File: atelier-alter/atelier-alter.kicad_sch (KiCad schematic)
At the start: 55 parts, among them SW1 SW_DPST, SW2 SW_DPST, SW3 SW_DPST, SW4 RESET, U1 ATmega32U4-A, U2 PRTR5V0U2X, Y1 16Mhz

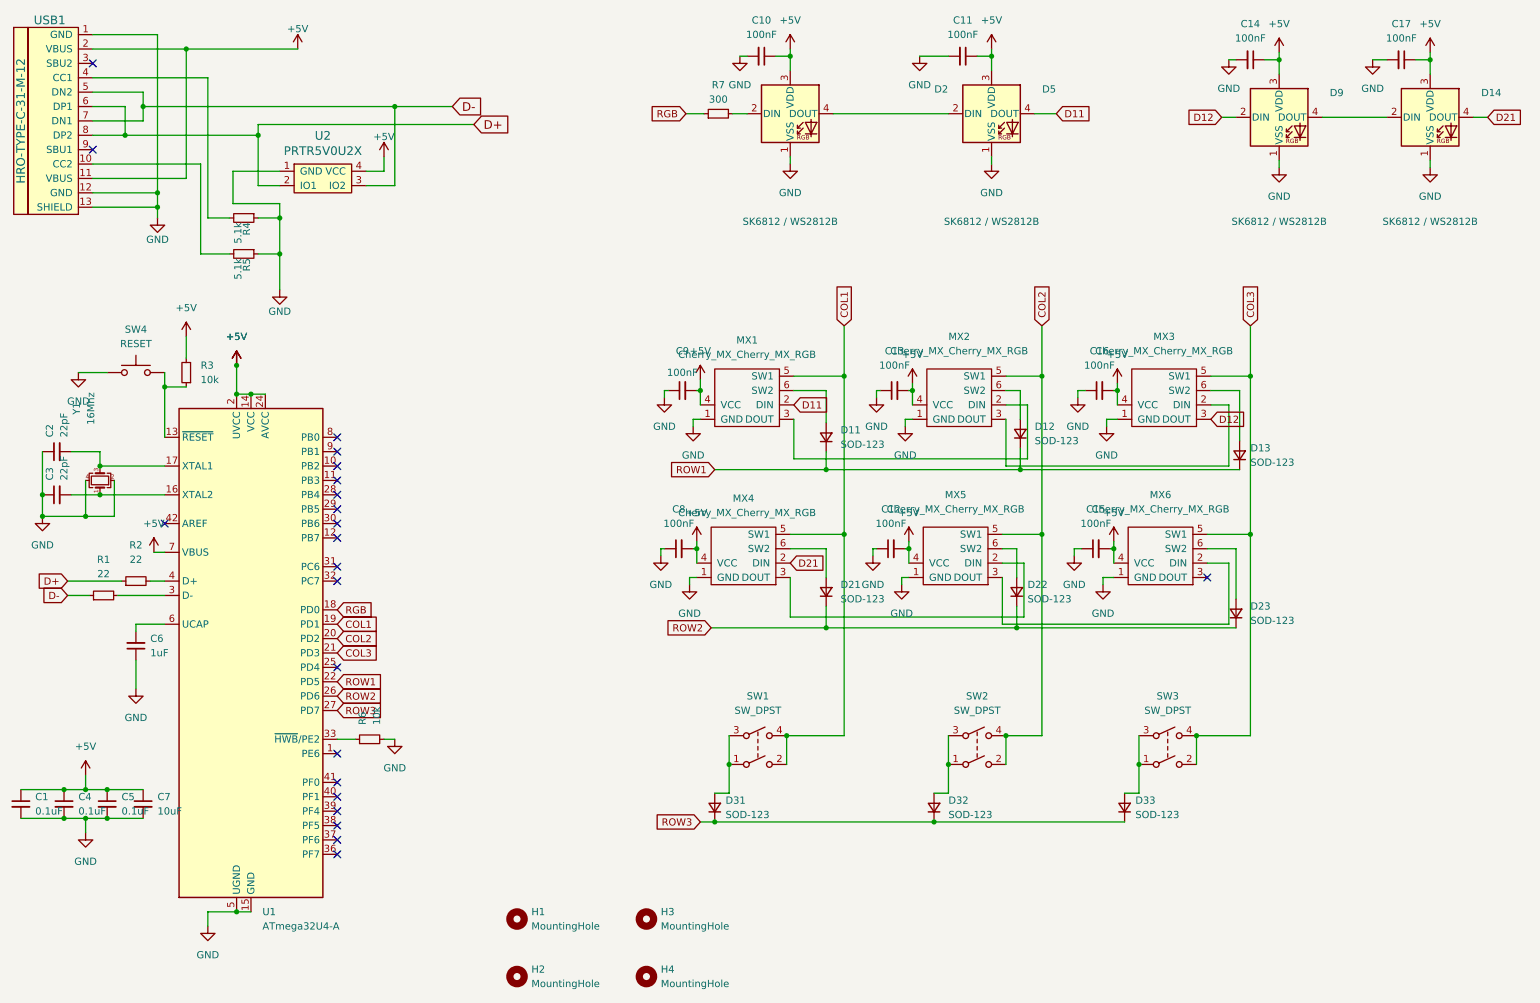
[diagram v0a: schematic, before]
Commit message: decided to nuke all led capacitor
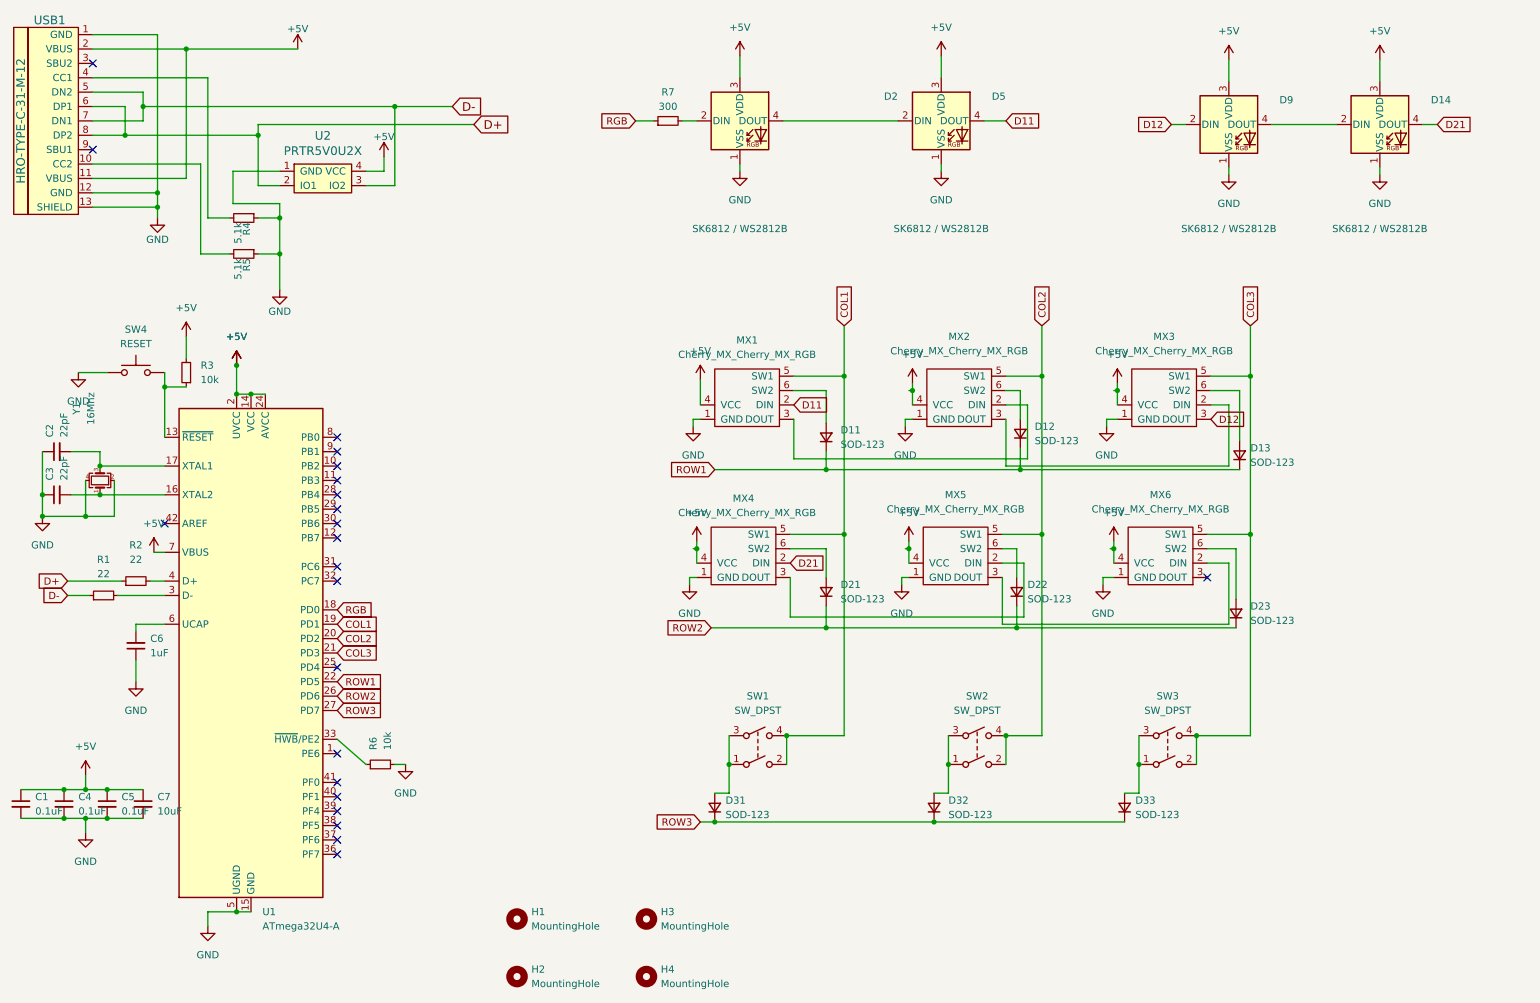
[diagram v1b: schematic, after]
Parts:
- removed C10, C11, C12, C13, C14, C15, C16, C17, C8, C9: 100nF, Capacitor_SMD:C_0805_2012Metric, symbol Device:C_Small
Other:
- moved on the sheet: D14, D2, D5, D9, R6, R7

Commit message: update pcb + qmk firmware
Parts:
- added R8: 300, Resistor_SMD:R_0805_2012Metric, symbol Device:R_Small
- renumbered D2 to D1, D5 to D2, D9 to D3, D14 to D4
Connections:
- net D12: now also MX4.2 (DIN); no longer D3.2 (DIN)
- net at U1.25 (PD4): now also R8.1
- net BackRGB: now reaches D1.2 (DIN)
- net BackRGB: now also R8.2; no longer R7.2
- net D11: no longer names the net of D2.4 (DOUT)
- net D11: now also D3.2 (DIN); no longer MX1.2 (DIN)
- net D21: no longer names the net of D4.4 (DOUT)
- net D21: no longer MX4.2 (DIN)
- net RGB: no longer names the net of R7.1, U1.18 (PD0)
- new net InKeyRGB: MX1.2 (DIN), R7.2
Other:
- moved on the sheet: D1, D3, D4

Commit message: final commit for rev 0.
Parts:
- H1, H2, H3, H4: footprint MountingHole:MountingHole_5.3mm_M5 -> MountingHole:MountingHole_3.2mm_M3_ISO7380
- R1, R2: footprint Resistor_SMD:R_0805_2012Metric -> Resistor_SMD:R_0603_1608Metric_Pad0.98x0.95mm_HandSolder
- SW1, SW2, SW3: footprint Button_Switch_THT:SW_PUSH_6mm_H9.5mm -> Button_Switch_THT:SW_PUSH_6mm_H13mm
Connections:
- net at U1.25 (PD4): no longer R8.1
- net at U1.28 (PB4): now also R8.1
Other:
- moved on the sheet: R8
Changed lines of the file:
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@@
   )
   (no_connect (at 31.75 40.64))
-  (no_connect (at 74.93 104.14))
   (no_connect (at 74.93 106.68))
   (no_connect (at 238.125 35.56))
+  (no_connect (at 74.93 132.08))
   (no_connect (at 74.93 152.4))
   (no_connect (at 44.45 106.68))
@@
   (no_connect (at 74.93 99.06))
   (no_connect (at 31.75 25.4))
+  (no_connect (at 74.93 104.14))
   (no_connect (at 228.6 116.205))
-  (no_connect (at 74.93 101.6))
   (wire (pts (xy 52.07 177.8) (xy 52.07 175.26))
     (stroke (width 0) (type default) (color 0 0 0 0))
@@
     (stroke (width 0) (type default) (color 0 0 0 0))
   )
+  (wire (pts (xy 76.835 101.6) (xy 74.93 101.6))
+    (stroke (width 0) (type default) (color 0 0 0 0))
+  )
   (wire (pts (xy 232.41 124.46) (xy 232.41 113.665))
     (stroke (width 0) (type default) (color 0 0 0 0))
@@
     (stroke (width 0) (type default) (color 0 0 0 0))
   )
-  (wire (pts (xy 86.995 132.08) (xy 83.185 132.08))
+  (wire (pts (xy 85.725 101.6) (xy 81.915 101.6))
     (stroke (width 0) (type default) (color 0 0 0 0))
   )
@@
   )
   (wire (pts (xy 180.34 154.305) (xy 182.88 154.305))
-    (stroke (width 0) (type default) (color 0 0 0 0))
-  )
-  (wire (pts (xy 78.105 132.08) (xy 74.93 132.08))
     (stroke (width 0) (type default) (color 0 0 0 0))
   )
@@
     )
   )
-  (global_label "BackRGB" (shape input) (at 86.995 132.08 0) (fields_autoplaced)
+  (global_label "BackRGB" (shape input) (at 85.725 101.6 0) (fields_autoplaced)
     (effects (font (size 1.27 1.27)) (justify left))
-    (property "Intersheet References" "${INTERSHEET_REFS}" (id 0) (at 97.7538 132.0006 0)
+    (property "Intersheet References" "${INTERSHEET_REFS}" (id 0) (at 96.4838 101.5206 0)
       (effects (font (size 1.27 1.27)) (justify left) hide)
     )
@@
     (property "Reference" "SW3" (id 0) (at 221.615 137.16 0))
     (property "Value" "SW_DPST" (id 1) (at 221.615 139.7 0))
-    (property "Footprint" "Button_Switch_THT:SW_PUSH_6mm_H9.5mm" (id 2) (at 221.615 146.685 0)
+    (property "Footprint" "Button_Switch_THT:SW_PUSH_6mm_H13mm" (id 2) (at 221.615 146.685 0)
       (effects (font (size 1.27 1.27)) hide)
     )
@@
       (effects (font (size 1.27 1.27)) (justify left))
     )
-    (property "Footprint" "MountingHole:MountingHole_5.3mm_M5" (id 2) (at 129.54 186.69 0)
+    (property "Footprint" "MountingHole:MountingHole_3.2mm_M3_ISO7380" (id 2) (at 129.54 186.69 0)
       (effects (font (size 1.27 1.27)) hide)
     )
@@
       (effects (font (size 1.27 1.27)) (justify left))
     )
-    (property "Footprint" "MountingHole:MountingHole_5.3mm_M5" (id 2) (at 106.68 186.69 0)
+    (property "Footprint" "MountingHole:MountingHole_3.2mm_M3_ISO7380" (id 2) (at 106.68 186.69 0)
       (effects (font (size 1.27 1.27)) hide)
     )
@@
     (property "Reference" "R2" (id 0) (at 39.37 110.49 90))
     (property "Value" "22" (id 1) (at 39.37 113.03 90))
-    (property "Footprint" "Resistor_SMD:R_0805_2012Metric" (id 2) (at 39.37 116.84 0)
+    (property "Footprint" "Resistor_SMD:R_0603_1608Metric_Pad0.98x0.95mm_HandSolder" (id 2) (at 39.37 116.84 0)
       (effects (font (size 1.27 1.27)) hide)
     )
@@
     (pin "1")
   )
-  (symbol (lib_id "Device:R_Small") (at 80.645 132.08 90) (unit 1)
+  (symbol (lib_id "Device:R_Small") (at 79.375 101.6 90) (unit 1)
     (in_bom yes) (on_board yes)
-    (property "Reference" "R8" (id 0) (at 80.645 127 90))
-    (property "Value" "300" (id 1) (at 80.645 129.54 90))
-    (property "Footprint" "Resistor_SMD:R_0805_2012Metric" (id 2) (at 80.645 132.08 0)
-      (effects (font (size 1.27 1.27)) hide)
-    )
-    (property "Datasheet" "~" (id 3) (at 80.645 132.08 0)
+    (property "Reference" "R8" (id 0) (at 79.375 96.52 90))
+    (property "Value" "300" (id 1) (at 79.375 99.06 90))
+    (property "Footprint" "Resistor_SMD:R_0805_2012Metric" (id 2) (at 79.375 101.6 0)
+      (effects (font (size 1.27 1.27)) hide)
+    )
+    (property "Datasheet" "~" (id 3) (at 79.375 101.6 0)
       (effects (font (size 1.27 1.27)) hide)
     )
@@
       (effects (font (size 1.27 1.27)) (justify left))
     )
-    (property "Footprint" "MountingHole:MountingHole_5.3mm_M5" (id 2) (at 106.68 176.53 0)
+    (property "Footprint" "MountingHole:MountingHole_3.2mm_M3_ISO7380" (id 2) (at 106.68 176.53 0)
       (effects (font (size 1.27 1.27)) hide)
     )
@@
       (effects (font (size 1.27 1.27)) (justify left))
     )
-    (property "Footprint" "MountingHole:MountingHole_5.3mm_M5" (id 2) (at 129.54 176.53 0)
+    (property "Footprint" "MountingHole:MountingHole_3.2mm_M3_ISO7380" (id 2) (at 129.54 176.53 0)
       (effects (font (size 1.27 1.27)) hide)
     )
@@
     (property "Reference" "SW1" (id 0) (at 149.225 137.16 0))
     (property "Value" "SW_DPST" (id 1) (at 149.225 139.7 0))
-    (property "Footprint" "Button_Switch_THT:SW_PUSH_6mm_H9.5mm" (id 2) (at 149.225 146.685 0)
+    (property "Footprint" "Button_Switch_THT:SW_PUSH_6mm_H13mm" (id 2) (at 149.225 146.685 0)
       (effects (font (size 1.27 1.27)) hide)
     )
@@
     (property "Reference" "R1" (id 0) (at 33.655 113.03 90))
     (property "Value" "22" (id 1) (at 33.655 115.57 90))
-    (property "Footprint" "Resistor_SMD:R_0805_2012Metric" (id 2) (at 33.655 119.38 0)
+    (property "Footprint" "Resistor_SMD:R_0603_1608Metric_Pad0.98x0.95mm_HandSolder" (id 2) (at 33.655 119.38 0)
       (effects (font (size 1.27 1.27)) hide)
     )
@@
     (property "Reference" "SW2" (id 0) (at 187.96 137.16 0))
     (property "Value" "SW_DPST" (id 1) (at 187.96 139.7 0))
-    (property "Footprint" "Button_Switch_THT:SW_PUSH_6mm_H9.5mm" (id 2) (at 187.96 146.685 0)
+    (property "Footprint" "Button_Switch_THT:SW_PUSH_6mm_H13mm" (id 2) (at 187.96 146.685 0)
       (effects (font (size 1.27 1.27)) hide)
     )
@@
     )
     (path "/8556b1bc-59f1-44d9-99ff-e1f2c0ffcf36"
-      (reference "H1") (unit 1) (value "MountingHole") (footprint "MountingHole:MountingHole_5.3mm_M5")
+      (reference "H1") (unit 1) (value "MountingHole") (footprint "MountingHole:MountingHole_3.2mm_M3_ISO7380")
     )
     (path "/5a99e80a-11b8-48d3-b554-660c0bcf5c38"
-      (reference "H2") (unit 1) (value "MountingHole") (footprint "MountingHole:MountingHole_5.3mm_M5")
+      (reference "H2") (unit 1) (value "MountingHole") (footprint "MountingHole:MountingHole_3.2mm_M3_ISO7380")
     )
     (path "/9a99f614-4356-46fa-a338-e647cb700704"
-      (reference "H3") (unit 1) (value "MountingHole") (footprint "MountingHole:MountingHole_5.3mm_M5")
+      (reference "H3") (unit 1) (value "MountingHole") (footprint "MountingHole:MountingHole_3.2mm_M3_ISO7380")
     )
     (path "/3b67de7c-1c99-408a-a31c-508b13725aa4"
-      (reference "H4") (unit 1) (value "MountingHole") (footprint "MountingHole:MountingHole_5.3mm_M5")
+      (reference "H4") (unit 1) (value "MountingHole") (footprint "MountingHole:MountingHole_3.2mm_M3_ISO7380")
     )
     (path "/92fbf038-747f-4dcc-ac4a-6dcc9e81a6d6"
@@
     )
     (path "/cab66ac1-fa01-4b4d-b047-bbf2c7667c4d"
-      (reference "R1") (unit 1) (value "22") (footprint "Resistor_SMD:R_0805_2012Metric")
+      (reference "R1") (unit 1) (value "22") (footprint "Resistor_SMD:R_0603_1608Metric_Pad0.98x0.95mm_HandSolder")
     )
     (path "/7a828e50-c71e-4f23-a75f-5b21626200ef"
-      (reference "R2") (unit 1) (value "22") (footprint "Resistor_SMD:R_0805_2012Metric")
+      (reference "R2") (unit 1) (value "22") (footprint "Resistor_SMD:R_0603_1608Metric_Pad0.98x0.95mm_HandSolder")
     )
     (path "/ab650c07-16c5-47e1-91d8-64187369346c"
@@
     )
     (path "/a25abf13-8d9c-45bf-8510-20336f41d055"
-      (reference "SW1") (unit 1) (value "SW_DPST") (footprint "Button_Switch_THT:SW_PUSH_6mm_H9.5mm")
+      (reference "SW1") (unit 1) (value "SW_DPST") (footprint "Button_Switch_THT:SW_PUSH_6mm_H13mm")
     )
     (path "/ecfd7051-baf1-4abd-8967-31e1a5902ed8"
-      (reference "SW2") (unit 1) (value "SW_DPST") (footprint "Button_Switch_THT:SW_PUSH_6mm_H9.5mm")
+      (reference "SW2") (unit 1) (value "SW_DPST") (footprint "Button_Switch_THT:SW_PUSH_6mm_H13mm")
     )
     (path "/09679efe-a303-405b-973d-0bd9043f5a9f"
-      (reference "SW3") (unit 1) (value "SW_DPST") (footprint "Button_Switch_THT:SW_PUSH_6mm_H9.5mm")
+      (reference "SW3") (unit 1) (value "SW_DPST") (footprint "Button_Switch_THT:SW_PUSH_6mm_H13mm")
     )
     (path "/91118ff8-7202-458d-979e-51942ec60b0d"
